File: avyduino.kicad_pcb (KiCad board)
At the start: 2 copper layers, 68.6 x 53.3 mm, 8 parts, among them J1 Power, J2 Digital/PWM, J3 Analog, J4 Digital/PWM

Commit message: do layout
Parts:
- added C1: 100nF, Capacitor_SMD:C_0805_2012Metric, F.Cu at (154.2, 60.5)
- added C10: 100nF, Capacitor_SMD:C_0805_2012Metric, F.Cu at (137.2, 55.5)
- added C11: 100nF, Capacitor_SMD:C_0805_2012Metric, F.Cu at (159.9, 60.5)
- added C12: 100nF, Capacitor_SMD:C_0805_2012Metric, F.Cu at (159.9, 65.2)
- added C13: 100nF, Capacitor_SMD:C_0805_2012Metric, F.Cu at (131.7, 70.8)
- added C14: 100nF, Capacitor_SMD:C_0805_2012Metric, F.Cu at (154.2, 70.5)
- added C2: 100nF, Capacitor_SMD:C_0805_2012Metric, F.Cu at (154.2, 65.5)
- added C3: 100nF, Capacitor_SMD:C_0805_2012Metric, F.Cu at (137.2, 70.8)
- added C4: 22pF, Capacitor_SMD:C_0805_2012Metric, F.Cu at (131.7, 65.5)
- added C5: 22pF, Capacitor_SMD:C_0805_2012Metric, F.Cu at (137.2, 65.5)
- added C6: 100nF, Capacitor_SMD:C_0805_2012Metric, F.Cu at (137.2, 60.5)
- added C7: 22pF, Capacitor_SMD:C_0805_2012Metric, F.Cu at (142.7, 70.8)
- added C8: 22pF, Capacitor_SMD:C_0805_2012Metric, F.Cu at (147.9, 70.8)
- added C9: 100nF, Capacitor_SMD:C_0805_2012Metric, F.Cu at (131.7, 60.5)
- added D1: D, Diode_THT:D_DO-35_SOD27_P10.16mm_Horizontal, F.Cu at (163.2, 55.0)
- added J5: USB_C_Receptacle_USB2.0_14P, Connector_USB:USB_C_Receptacle_GCT_USB4105-xx-A_16P_TopMnt_Horizontal, F.Cu at (104.6, 61.8)
- added Q1: AO3401A, Package_TO_SOT_SMD:SOT-23, F.Cu at (117.5, 57.7)
- added R1: 10k, Resistor_SMD:R_0805_2012Metric, F.Cu at (142.7, 55.5)
- added R2: 1m, Resistor_SMD:R_0805_2012Metric, F.Cu at (142.7, 65.5)
- added R3: 5.1k, Resistor_SMD:R_0805_2012Metric, F.Cu at (142.7, 60.5)
- added R4: 5.1k, Resistor_SMD:R_0805_2012Metric, F.Cu at (147.9, 65.5)
- added R5: 10k, Resistor_SMD:R_0805_2012Metric, F.Cu at (147.9, 55.5)
- added R6: 10k, Resistor_SMD:R_0805_2012Metric, F.Cu at (147.9, 60.5)
- added U1: ATmega328P-P, Package_DIP:DIP-28_W7.62mm_Socket_LongPads, F.Cu at (163.4, 79.6)
- added U2: CH340G, Package_SO:SOIC-16_3.9x9.9mm_P1.27mm, F.Cu at (124.5, 58.4)
- added U3: LM2931AZ-5.0_TO92, Package_TO_SOT_THT:TO-92_Inline, F.Cu at (121.7, 72.2)
- added U4: MCP1700x-330xxTT, Package_TO_SOT_SMD:SOT-23, F.Cu at (117.4, 64.2)
- added U5: LM358, Package_DIP:DIP-8_W7.62mm_Socket_LongPads, F.Cu at (116.4, 85.2)
- added Y1: 12MHz, Crystal:Crystal_HC49-U_Vertical, F.Cu at (106.2, 73.8)
- added Y2: 16MHz, Crystal:Crystal_HC49-U_Vertical, F.Cu at (115.2, 78.6)
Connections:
- J1 pad 2: /IOREF -> +5V
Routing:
- net GND: track 0.00 -> 11.1 mm

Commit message: route the pcb. will add some cool silkscreen
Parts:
- moved U1 0.25 mm to (163.6, 79.6)
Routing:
- net +5V: track 0.00 -> 154.3 mm, vias 0 -> 15
- net /SCL/A5: track 0.00 -> 116.2 mm, vias 0 -> 5
- net /*10: track 0.00 -> 105.9 mm, vias 0 -> 3
- net /SDA/A4: track 0.00 -> 88.5 mm, vias 0 -> 1
- net /~{RESET}: track 0.00 -> 88.0 mm, vias 0 -> 5
- net /RX/0: track 0.00 -> 77.8 mm, vias 0 -> 2
- net /TX/1: track 0.00 -> 77.4 mm, vias 0 -> 5
- net Net-(U5A--): track 0.00 -> 68.7 mm, vias 0 -> 6
- net Net-(J5-CC1): track 0.00 -> 67.6 mm, vias 0 -> 5
- net /13: track 0.00 -> 61.6 mm, vias 0 -> 1
- net /AREF: track 0.00 -> 60.3 mm, vias 0 -> 3
- net /12: track 0.00 -> 58.7 mm, vias 0 -> 4
- net /*11: track 0.00 -> 58.0 mm, vias 0 -> 5
- net VBUS: track 0.00 -> 55.2 mm, vias 0 -> 2
- net +3V3: track 0.00 -> 51.4 mm, vias 0 -> 3
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- added copper zone on B.Cu, net GND
- added copper zone on F.Cu, net VCC

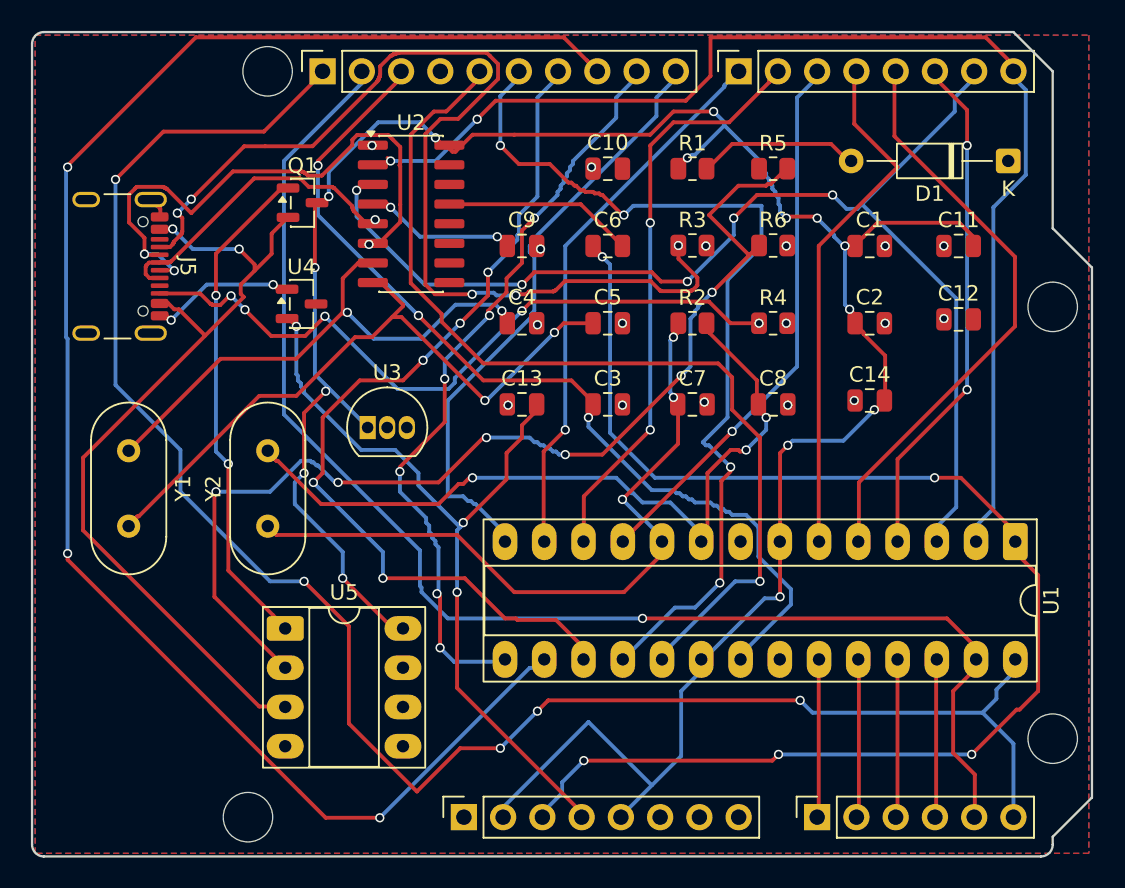
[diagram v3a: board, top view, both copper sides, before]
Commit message: routed ICSP header
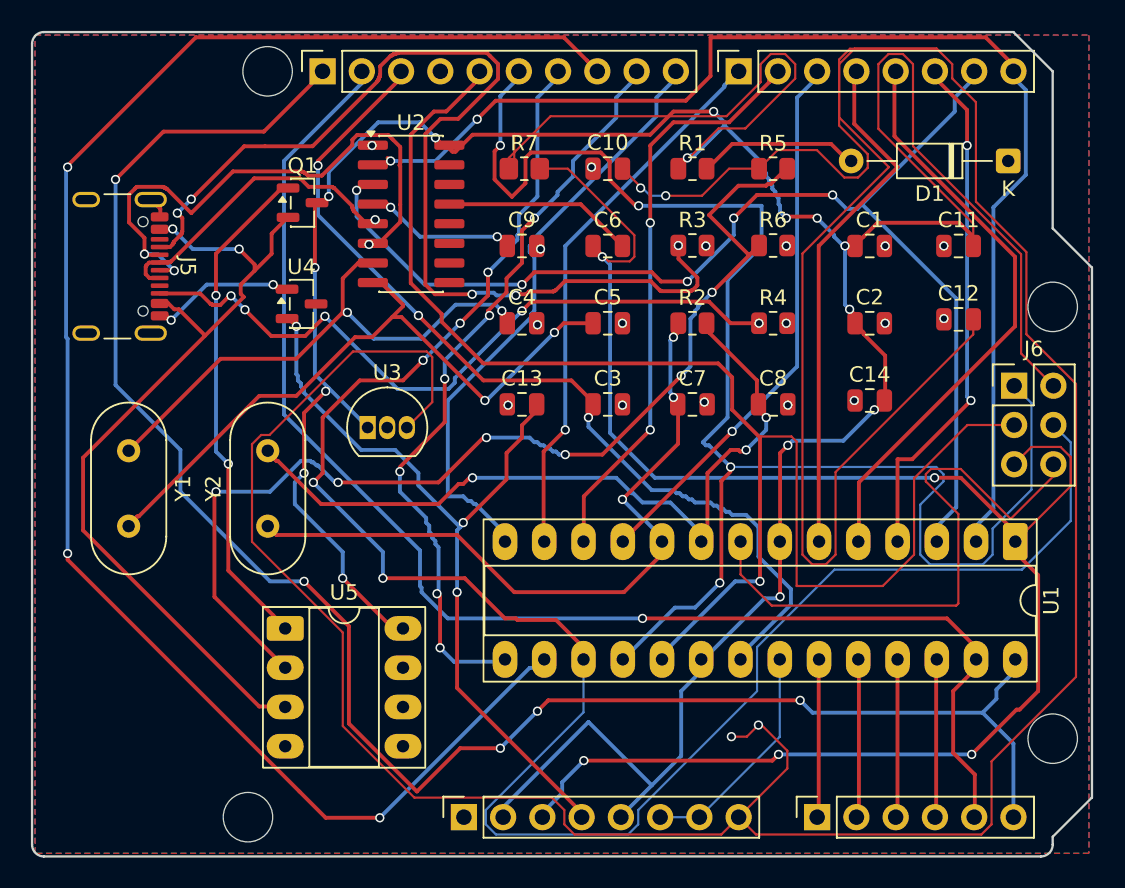
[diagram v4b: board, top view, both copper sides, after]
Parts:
- added J6: ICSP Header, Connector_PinHeader_2.54mm:PinHeader_2x03_P2.54mm_Vertical, F.Cu at (163.5, 69.5)
- added R7: 10k, Resistor_SMD:R_0805_2012Metric_Pad1.20x1.40mm_HandSolder, F.Cu at (131.8, 55.5)
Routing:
- net VCC: track 0.00 -> 250.2 mm, vias 0 -> 4
- net +5V: track 154.3 -> 232.2 mm
- net /*11: track 58.0 -> 126.7 mm
- net GND: track 14.0 -> 66.9 mm
- net /12: track 58.7 -> 101.6 mm
- net /13: track 61.6 -> 94.7 mm
- net /~{RESET}: track 88.0 -> 111.9 mm
- net /2: track 32.8 -> 33.5 mm

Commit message: redo layout of pcb
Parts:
- D1: value D -> Diode
- J1: value Power -> Power Header
- J2, J4: value Digital/PWM -> Digital/PWM Header
- J3: value Analog -> Analog Header
- U4: value MCP1700x-330xxTT -> MCP1700x-330xxTO; footprint Package_TO_SOT_SMD:SOT-23 -> Package_TO_SOT_THT:TO-92_Inline
- moved R4 40.2 mm to (108.0, 70.0)
- moved Y1 39.4 mm to (144.2, 63.3)
- moved R7 36.9 mm to (128.5, 92.2)
- moved R3 35.3 mm to (108.0, 54.0)
- moved C12 34.0 mm to (139.2, 92.2)
- moved C6 31.9 mm to (133.9, 92.2)
- moved C8 31.9 mm to (121.5, 88.5)
- moved U3 30.6 mm to (152.2, 73.5)
- moved U5 28.3 mm to (115.1, 57.0)
- moved R2 25.0 mm to (121.5, 78.8)
- moved C7 24.8 mm to (121.5, 83.6)
- moved C10 23.7 mm to (159.4, 63.8)
- moved C1 23.1 mm to (132.0, 54.0)
- moved C3 22.7 mm to (144.6, 92.2)
- moved U4 21.8 mm to (137.2, 73.5)
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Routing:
- net VCC: track 250.2 -> 0.00 mm, vias 4 -> 0
- net +5V: track 232.2 -> 0.00 mm, vias 15 -> 0
- net /*11: track 126.7 -> 0.00 mm, vias 5 -> 0
- net /SCL/A5: track 116.2 -> 0.00 mm, vias 5 -> 0
- net /~{RESET}: track 111.9 -> 0.00 mm, vias 5 -> 0
- net /*10: track 105.9 -> 0.00 mm, vias 3 -> 0
- net /12: track 101.6 -> 0.00 mm, vias 4 -> 0
- net /13: track 94.7 -> 0.00 mm, vias 1 -> 0
- net /SDA/A4: track 88.5 -> 0.00 mm, vias 1 -> 0
- net /RX/0: track 77.8 -> 0.00 mm, vias 2 -> 0
- net /TX/1: track 77.4 -> 0.00 mm, vias 5 -> 0
- net Net-(U5A--): track 68.7 -> 0.00 mm, vias 6 -> 0
- net Net-(J5-CC1): track 67.6 -> 0.00 mm, vias 5 -> 0
- net GND: track 66.9 -> 0.00 mm, vias 19 -> 0
- net /AREF: track 60.3 -> 0.00 mm, vias 3 -> 0
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- removed copper zone on F.Cu, net VCC

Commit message: route pcb and make BOMs
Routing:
- net /13: track 0.00 -> 164.1 mm, vias 0 -> 2
- net +5V: track 0.00 -> 134.0 mm, vias 0 -> 12
- net /12: track 0.00 -> 122.9 mm, vias 0 -> 4
- net /SCL/A5: track 0.00 -> 118.4 mm, vias 0 -> 6
- net /SDA/A4: track 0.00 -> 97.9 mm, vias 0 -> 5
- net /*11: track 0.00 -> 93.2 mm, vias 0 -> 4
- net /AREF: track 0.00 -> 86.9 mm, vias 0 -> 2
- net /TX/1: track 0.00 -> 79.7 mm, vias 0 -> 2
- net VCC: track 0.00 -> 72.2 mm, vias 0 -> 6
- net Net-(U5A--): track 0.00 -> 65.9 mm, vias 0 -> 2
- net /*9: track 0.00 -> 60.3 mm, vias 0 -> 6
- net /~{RESET}: track 0.00 -> 59.8 mm, vias 0 -> 1
- net /RX/0: track 0.00 -> 59.1 mm, vias 0 -> 4
- net /*10: track 0.00 -> 50.8 mm, vias 0 -> 4
- net /UD-: track 0.00 -> 49.1 mm, vias 0 -> 2
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
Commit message: redo layout and add reset button
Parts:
- added G***: LOGO, silkscreen:dinohat, B.Cu at (119.5, 64.2)
- added SW1: ~{RESET}, Button_Switch_THT:SW_PUSH_6mm, F.Cu at (102.7, 48.7)
- moved C12 34.3 mm to (159.0, 64.2)
- moved C8 26.8 mm to (144.0, 74.0)
- moved C6 24.3 mm to (136.0, 68.0)
- moved C7 23.5 mm to (144.0, 77.0)
- moved C1 23.1 mm to (154.0, 61.0)
- moved C2 22.9 mm to (132.6, 53.0)
- moved C13 22.7 mm to (138.8, 92.7)
- moved C9 9.88 mm to (129.0, 59.8)
- moved C4 7.21 mm to (129.0, 69.2)
- moved C10 5.37 mm to (159.0, 69.1)
- moved R3 5.34 mm to (113.3, 53.1), turned to 90 degrees
- moved C11 5.13 mm to (159.0, 59.4)
- moved C14 4.53 mm to (159.0, 54.5)
- moved C3 3.42 mm to (147.9, 92.7)
- moved Q1 2.68 mm to (128.0, 53.8)
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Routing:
- net /~{RESET}: track 59.8 -> 168.5 mm, vias 1 -> 14
- net /13: track 164.1 -> 91.3 mm, vias 2 -> 7
- net GND: track 42.1 -> 0.00 mm, vias 14 -> 77
- net /*5: track 37.8 -> 70.1 mm, vias 0 -> 4
- net /DTR: track 43.1 -> 12.5 mm, vias 6 -> 0
- net /*9: track 60.3 -> 88.5 mm, vias 6 -> 2
- net /12: track 122.9 -> 98.8 mm
- net /AREF: track 86.9 -> 108.5 mm, vias 2 -> 6
- net +5V: track 134.0 -> 154.9 mm, vias 12 -> 13
- net /SCL/A5: track 118.4 -> 100.2 mm, vias 6 -> 4
- net /UD-: track 49.1 -> 31.3 mm, vias 2 -> 0
- net /TX/1: track 79.7 -> 64.4 mm, vias 2 -> 3
- net Net-(U5A--): track 65.9 -> 54.1 mm, vias 2 -> 6
- net /XTAL2: track 36.7 -> 47.9 mm
- net /UD+: track 33.3 -> 41.7 mm, vias 2 -> 3
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- added copper zone on F.Cu, net GND
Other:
- board text added: "By Avy (avycado13) 13 Oct 2026"

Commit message: redo layout
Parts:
- moved C11 56.6 mm to (117.5, 97.9)
- moved C10 46.4 mm to (122.6, 97.9)
- moved R6 41.3 mm to (117.6, 85.1), turned to 180 degrees
- moved U3 37.7 mm to (119.2, 91.8)
- moved R7 36.5 mm to (158.5, 70.5)
- moved R5 35.9 mm to (123.2, 85.1), turned to 180 degrees
- moved C14 35.6 mm to (123.5, 56.8), turned to 180 degrees
- moved Q1 35.0 mm to (103.2, 78.5), turned to 180 degrees
- moved R2 34.9 mm to (154.2, 70.5), turned to 0 degrees
- moved C13 32.4 mm to (148.2, 61.7)
- moved C2 30.9 mm to (154.2, 75.0)
- moved Y2 29.6 mm to (139.6, 69.0), turned to 0 degrees
- moved C6 22.6 mm to (158.5, 65.8)
- moved U4 21.3 mm to (149.2, 55.9)
- moved U2 20.8 mm to (115.2, 61.2)
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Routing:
- net /13: track 91.3 -> 143.9 mm, vias 7 -> 5
- net /*9: track 88.5 -> 42.3 mm
- net /DTR: track 12.5 -> 57.5 mm, vias 0 -> 2
- net Net-(U5A--): track 54.1 -> 17.0 mm, vias 6 -> 0
- net /AREF: track 108.5 -> 72.7 mm, vias 6 -> 3
- net /UD+: track 41.7 -> 7.81 mm, vias 3 -> 0
- net /RX/0: track 64.2 -> 96.4 mm, vias 3 -> 4
- net /*5: track 70.1 -> 38.5 mm, vias 4 -> 1
- net /~{RESET}: track 168.5 -> 141.4 mm, vias 14 -> 6
- net /UD-: track 31.3 -> 8.97 mm, vias 0 -> 2
- net /TX/1: track 64.4 -> 84.2 mm, vias 3 -> 4
- net /XTAL2: track 47.9 -> 29.6 mm, vias 3 -> 2
- net VCC: track 69.8 -> 85.9 mm
- net +3V3: track 45.0 -> 59.9 mm, vias 1 -> 0
- net /*11: track 89.8 -> 78.9 mm, vias 3 -> 4
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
